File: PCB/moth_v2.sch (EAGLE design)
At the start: 86 parts, among them Q1 PNO8l07

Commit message: got a working version of the VEML sensors working through the TCA9543A
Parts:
- removed CTRL1, CTRL2, CTRL3: (no value), SparkFun-Connectors:CONN_03
- removed D2, D3, D5, D6: (no value), SparkFun-LED:LED-FKIT-1206
- removed LED_ON: (no value), SparkFun-Connectors:CONN_021X02_NO_SILK
- removed R10, R11, R17, R18: 4.7k, SparkFun-Resistors:4.7KOHM-0603-1/10W-1%
- removed R12, R14: 2k, adafruit:R-US_0207/10
- removed R15, R16: 10k, SparkFun-Resistors:10KOHM-0603-1/10W-1%
- removed U$2: BSS138, nathans-custom-parts:BSS138
- C1, C15, C2, C21: value 100nf -> 0.1uf
- NC1, NC10, NC11, NC12, NC2, NC3, NC4, NC5, NC6, NC7, NC8, NC9: value 1uf -> 0.1uf
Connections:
- removed net N$15: R14.1, U$3.GPIO22/GEN3
- removed net N$16: D2.A, R10.2
- removed net N$17: CTRL2.2, R14.2
- removed net N$18: CTRL1.2, R12.2
- removed net N$27: LED_ON.1, R10.1
- removed net N$28: D3.C, R11.2
- removed net N$29: D5.C, R17.2
- removed net N$3: R12.1, U$3.GPIO17/GEN0
- removed net N$30: D6.C, R18.2
- removed net N$32: D3.A, U$3.GEN4/GPIO23
- removed net N$33: D5.A, U$3.GEN5/GPIO24
- removed net N$34: D6.A, U$3.GEN/6GPIO25
- net 3.3V: no longer CTRL1.3, CTRL2.3, R16.1, U$2.G
- net 5V: no longer CTRL3.1, LED_ON.2, R15.2
- net GND: no longer CTRL1.1, CTRL2.1, CTRL3.3, D2.C, R11.1, R17.1, R18.1
- net NEO_P: no longer R16.2, U$2.S
- net NEO_P_CTRL: no longer CTRL3.2, R15.1, U$2.D
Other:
- note added: "Keep the I2C jst connectors for test points, but do not populate with parts?"
- note added: "replace 10uf cap with 1206"
- note removed: "2.2k"
- note removed: "Two generic header selection "buttons""

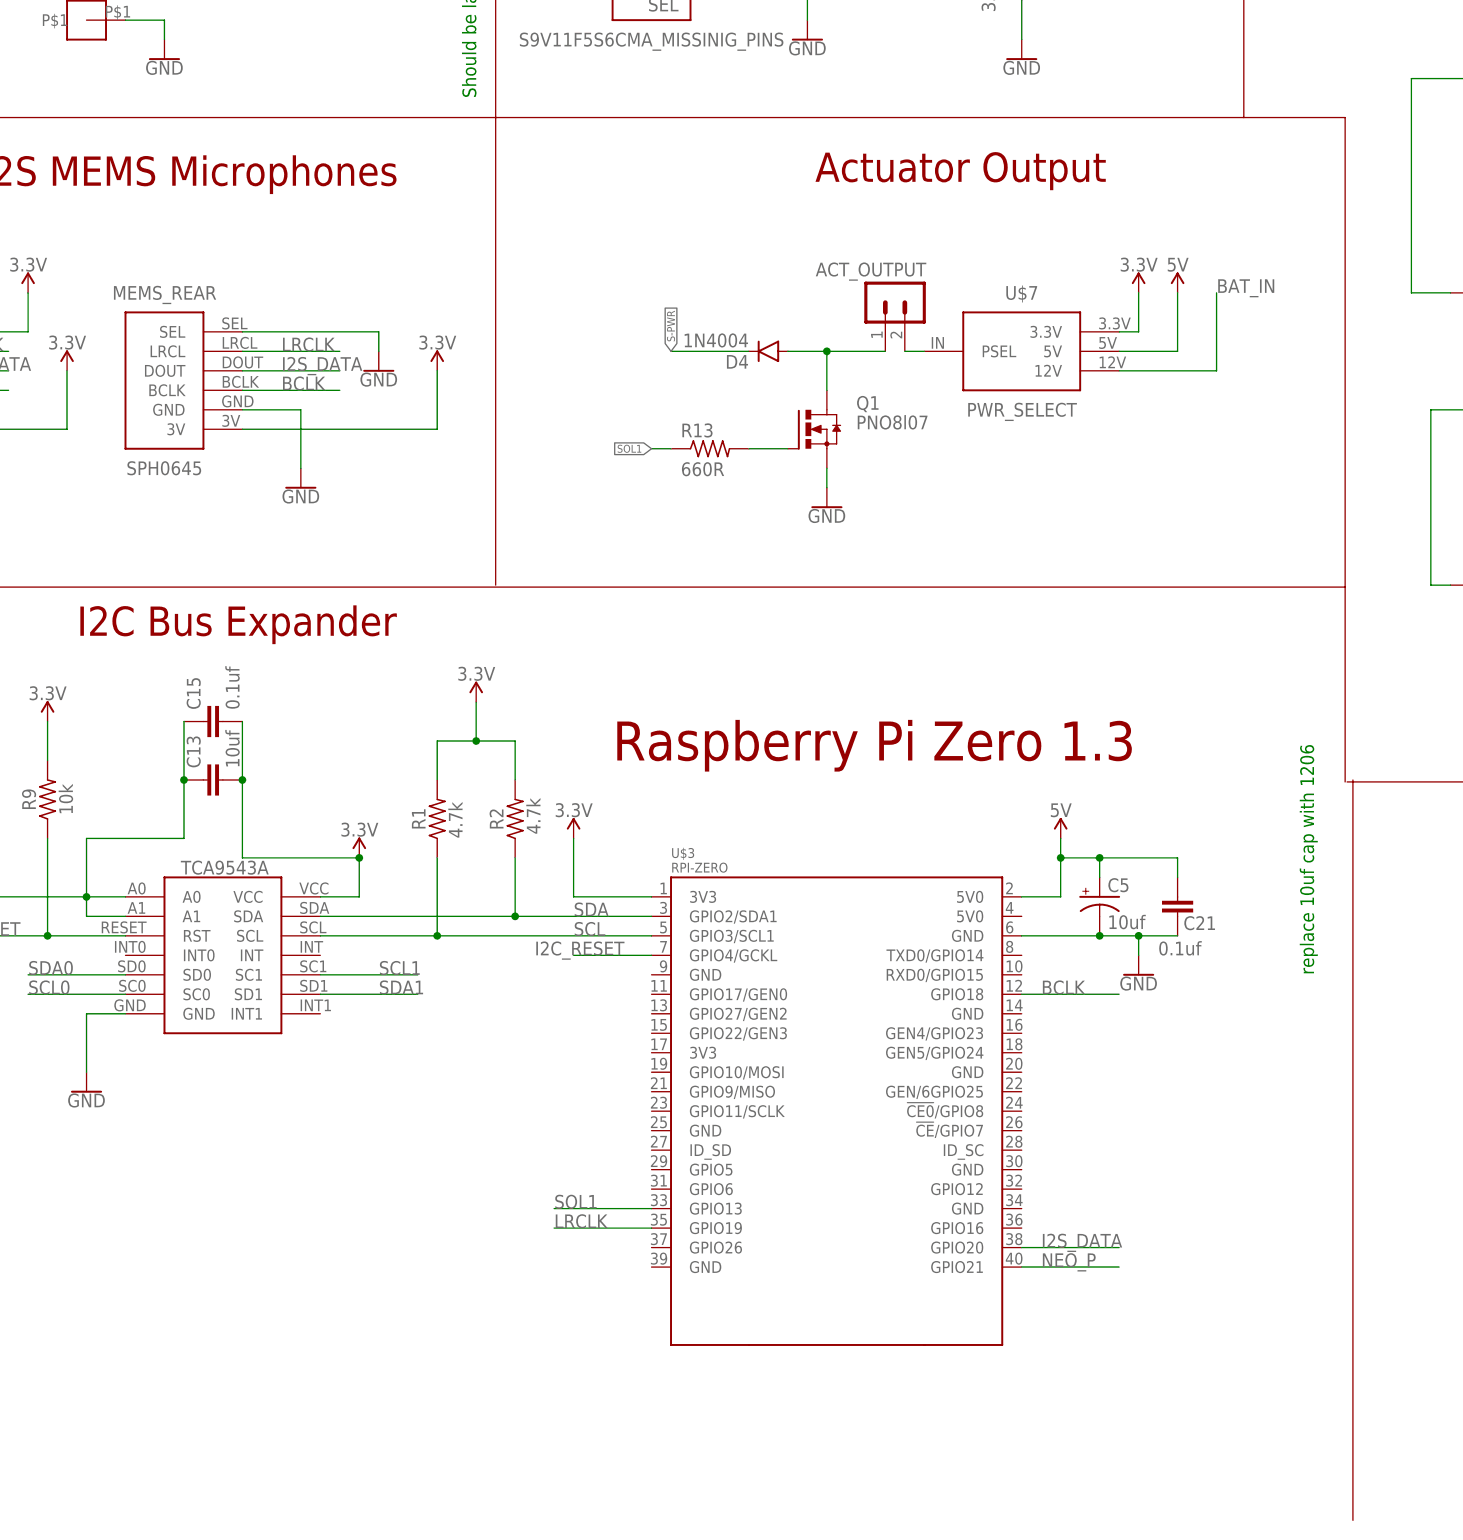
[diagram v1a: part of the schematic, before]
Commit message: new but untested auto_gain control also minor updates to the v2 PCB
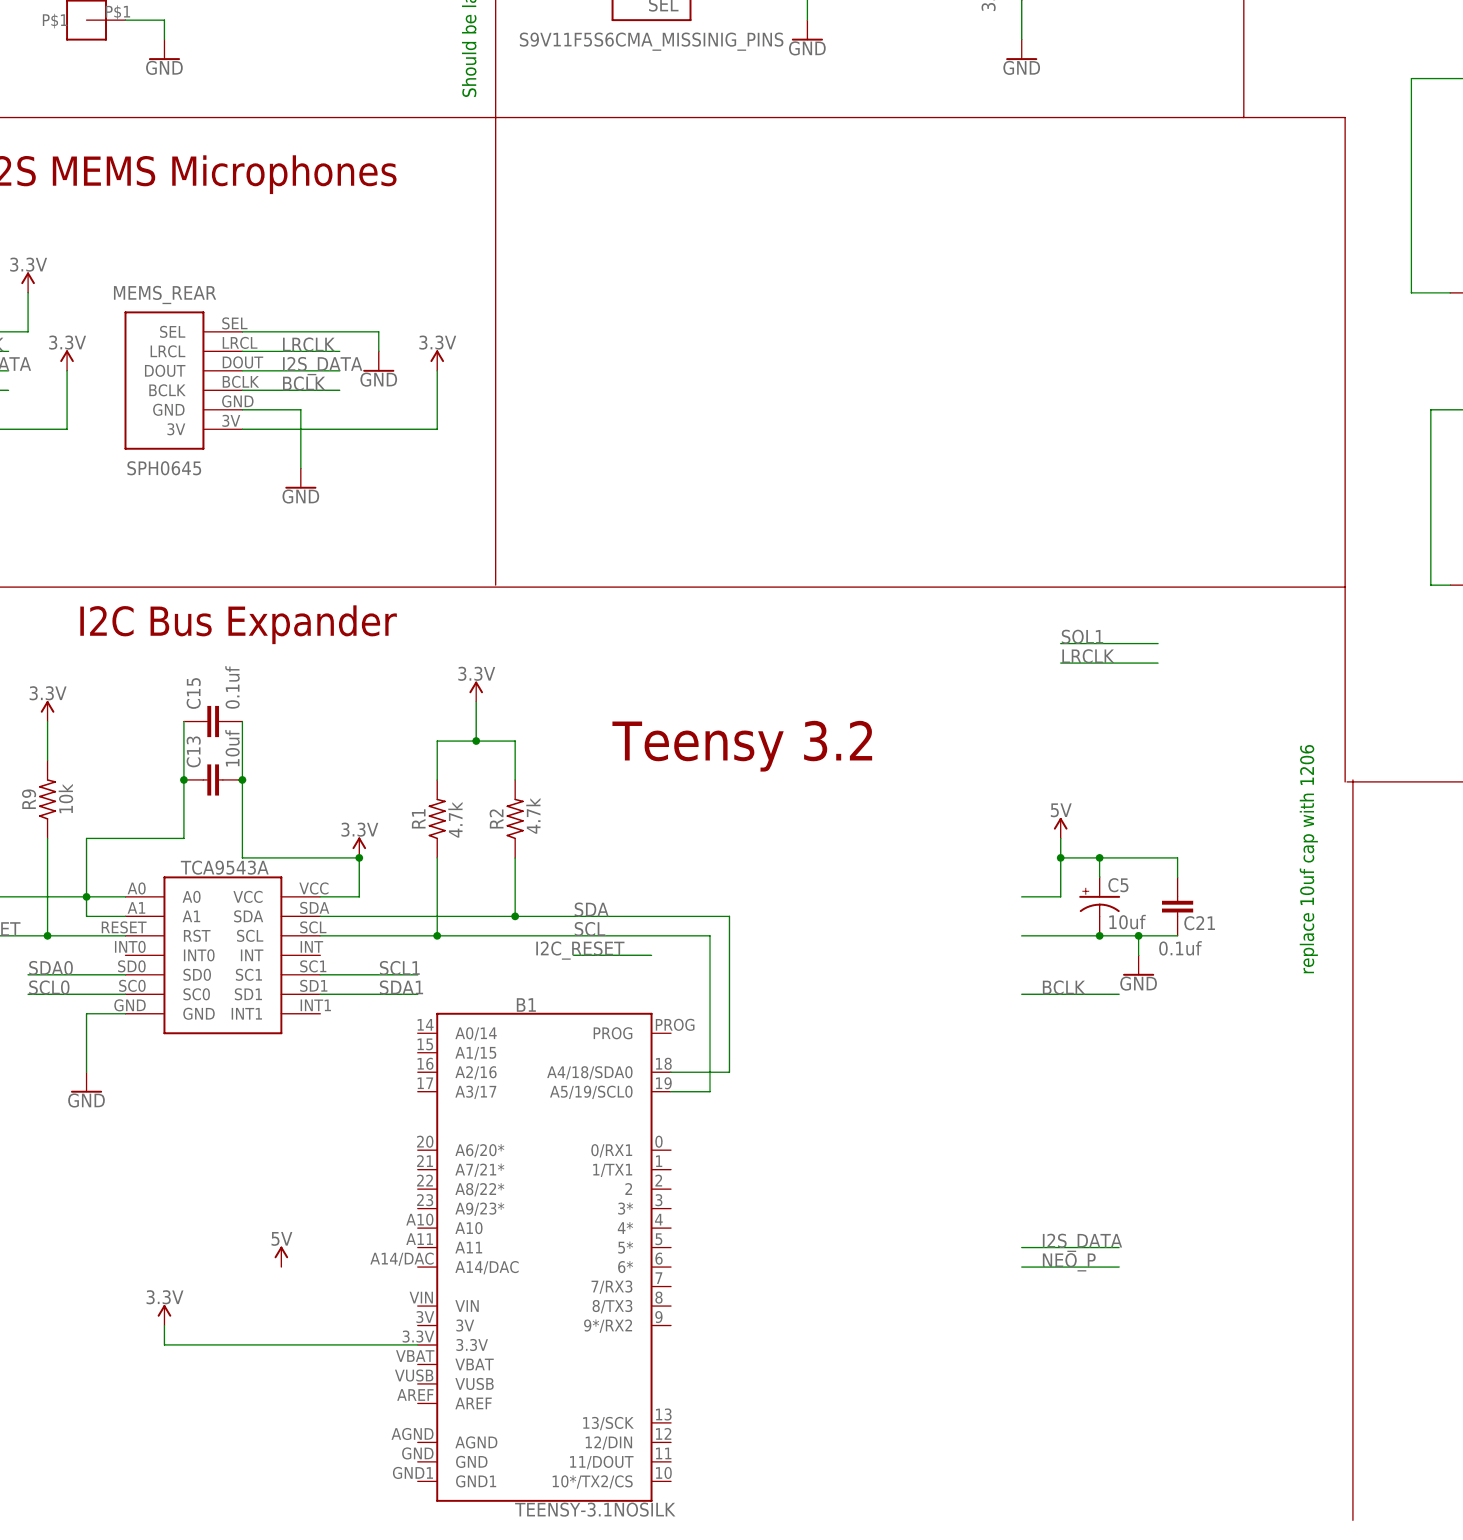
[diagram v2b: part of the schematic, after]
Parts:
- removed ACT_OUTPUT: B2B-PH-K, con-jst-ph:B2B-PH-K
- removed D4: 1N4004, SparkFun-DiscreteSemi:DIODEPTH
- removed Q1: PNO8l07, transistor-power:IRF3704-H
- removed R13: 660R, adafruit:R-US_0207/10
- removed U$3: RPI-ZERO, RPI-Zero:RPI-ZERO
- removed U$7: PWR_SELECT, nathans-custom-parts:PWR_SELECT
- added B1: TEENSY-3.1NOSILK, SparkFun-Boards:TEENSY-3.1NOSILK
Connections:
- removed net N$19: Q1.G, R13.2
- removed net N$20: ACT_OUTPUT.1, D4.A, Q1.D
- removed net NEO_P: U$3.GPIO21
- removed net S-PWR: ACT_OUTPUT.2, D4.C, U$7.PSEL
- removed net SOL1: R13.1, U$3.GPIO13
- net 3.3V: now also B1.3.3V; no longer U$3.3V3@1, U$7.3.3V
- net 5V: no longer U$3.5V0@1, U$7.5V
- net BAT_IN: no longer U$7.12V
- net BCLK: no longer U$3.GPIO18
- net GND: no longer Q1.S, U$3.GND@8
- net I2C_RESET: no longer U$3.GPIO4/GCKL
- net I2S_DATA: no longer U$3.GPIO20
- net LRCLK: no longer U$3.GPIO19
- net SCL: now also B1.A5/19/SCL0; no longer U$3.GPIO3/SCL1
- net SDA: now also B1.A4/18/SDA0; no longer U$3.GPIO2/SDA1
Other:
- note added: "Teensy 3.2"
- note removed: "660R"
- note removed: "Actuator Output"
- note removed: "Raspberry Pi Zero 1.3"
